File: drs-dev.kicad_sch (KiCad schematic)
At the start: 32 parts, among them J1 Conn_01x03_Pin, J2 USB_C_Receptacle_USB2.0_16P, J3 Conn_ARM_SWD_TagConnect_TC203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, J4 Conn_01x03_Pin, J5 Conn_01x03_Pin, J6 Conn_01x03_Pin, J7 Barrel_Jack_Switch, U4 SRV05-4, U5 STM32F103C8Tx, U6 AMS1117-3.3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

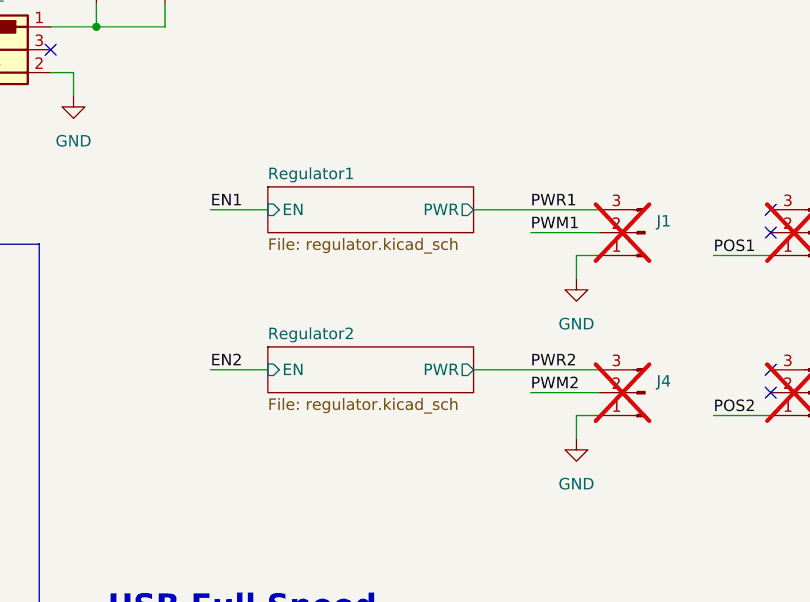
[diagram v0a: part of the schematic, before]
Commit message: Add labels and fix pinout
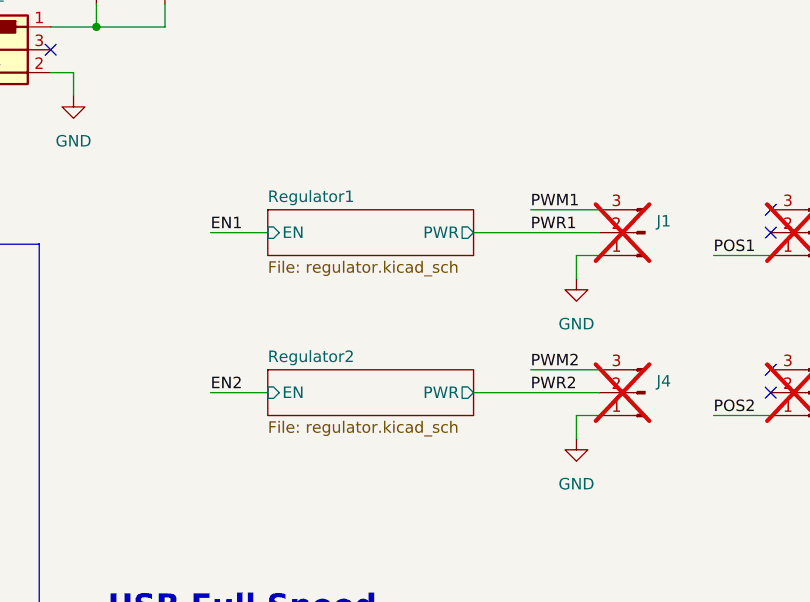
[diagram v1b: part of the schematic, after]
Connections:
- net PWM1: now also J1.3 (Pin_3); no longer J1.2 (Pin_2)
- net PWM2: now also J4.3 (Pin_3); no longer J4.2 (Pin_2)
- net PWR1: now also J1.2 (Pin_2); no longer J1.3 (Pin_3)
- net PWR2: now also J4.2 (Pin_2); no longer J4.3 (Pin_3)
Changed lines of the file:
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@@
 	(wire
 		(pts
-			(xy 187.96 69.85) (xy 195.58 69.85)
-		)
-		(stroke
-			(width 0)
-			(type default)
-		)
-	)
-	(wire
-		(pts
 			(xy 137.16 36.83) (xy 137.16 34.29)
 		)
@@
 	(wire
 		(pts
-			(xy 181.61 67.31) (xy 195.58 67.31)
+			(xy 181.61 69.85) (xy 195.58 69.85)
 		)
 		(stroke
@@
 	(wire
 		(pts
-			(xy 187.96 52.07) (xy 195.58 52.07)
+			(xy 187.96 49.53) (xy 195.58 49.53)
 		)
 		(stroke
@@
 	(wire
 		(pts
+			(xy 187.96 67.31) (xy 195.58 67.31)
+		)
+		(stroke
+			(width 0)
+			(type default)
+		)
+	)
+	(wire
+		(pts
 			(xy 40.64 166.37) (xy 48.26 166.37)
 		)
@@
 	(wire
 		(pts
-			(xy 181.61 49.53) (xy 195.58 49.53)
+			(xy 181.61 52.07) (xy 195.58 52.07)
 		)
 		(stroke
@@
 	(wire
 		(pts
-			(xy 152.4 49.53) (xy 158.75 49.53)
+			(xy 152.4 52.07) (xy 158.75 52.07)
 		)
 		(stroke
@@
 	(wire
 		(pts
-			(xy 152.4 67.31) (xy 158.75 67.31)
+			(xy 152.4 69.85) (xy 158.75 69.85)
 		)
 		(stroke
@@
 		)
 	)
-	(label "PWM2"
-		(at 187.96 69.85 0)
-		(fields_autoplaced yes)
-		(effects
-			(font
-				(size 1.27 1.27)
-			)
-			(justify left bottom)
-		)
-	)
 	(label "PWM1"
-		(at 187.96 52.07 0)
+		(at 187.96 49.53 0)
 		(fields_autoplaced yes)
 		(effects
@@
 	)
 	(label "PWR1"
-		(at 187.96 49.53 0)
+		(at 187.96 52.07 0)
 		(fields_autoplaced yes)
 		(effects
@@
 		)
 	)
+	(label "PWM2"
+		(at 187.96 67.31 0)
+		(fields_autoplaced yes)
+		(effects
+			(font
+				(size 1.27 1.27)
+			)
+			(justify left bottom)
+		)
+	)
 	(label "USB_D+"
 		(at 207.01 137.16 0)
@@
 	)
 	(label "PWR2"
-		(at 187.96 67.31 0)
+		(at 187.96 69.85 0)
 		(fields_autoplaced yes)
 		(effects
@@
 	)
 	(label "EN1"
-		(at 152.4 49.53 0)
+		(at 152.4 52.07 0)
 		(fields_autoplaced yes)
 		(effects
@@
 	)
 	(label "EN2"
-		(at 152.4 67.31 0)
+		(at 152.4 69.85 0)
 		(fields_autoplaced yes)
 		(effects
@@
 	)
 	(sheet
-		(at 158.75 46.99)
+		(at 158.75 49.53)
 		(size 22.86 5.08)
 		(fields_autoplaced yes)
@@
 		)
 		(property "Sheetname" "Regulator1"
-			(at 158.75 46.2784 0)
+			(at 158.75 48.8184 0)
 			(effects
 				(font
@@
 		)
 		(property "Sheetfile" "regulator.kicad_sch"
-			(at 158.75 52.6546 0)
+			(at 158.75 55.1946 0)
 			(effects
 				(font
@@
 		)
 		(pin "EN" input
-			(at 158.75 49.53 180)
+			(at 158.75 52.07 180)
 			(effects
 				(font
@@
 		)
 		(pin "PWR" output
-			(at 181.61 49.53 0)
+			(at 181.61 52.07 0)
 			(effects
 				(font
@@
 		)
 		(instances
-			(project "aero-dev"
+			(project "drs-dev"
 				(path "/66932111-2507-475e-a4ae-78de41b9a81d"
 					(page "2")
@@
 	)
 	(sheet
-		(at 158.75 64.77)
+		(at 158.75 67.31)
 		(size 22.86 5.08)
 		(fields_autoplaced yes)
@@
 		)
 		(property "Sheetname" "Regulator2"
-			(at 158.75 64.0584 0)
+			(at 158.75 66.5984 0)
 			(effects
 				(font
@@
 		)
 		(property "Sheetfile" "regulator.kicad_sch"
-			(at 158.75 70.4346 0)
+			(at 158.75 72.9746 0)
 			(effects
 				(font
@@
 		)
 		(pin "EN" input
-			(at 158.75 67.31 180)
+			(at 158.75 69.85 180)
 			(effects
 				(font
@@
 		)
 		(pin "PWR" output
-			(at 181.61 67.31 0)
+			(at 181.61 69.85 0)
 			(effects
 				(font
@@
 		)
 		(instances
-			(project "aero-dev"
+			(project "drs-dev"
 				(path "/66932111-2507-475e-a4ae-78de41b9a81d"
 					(page "3")

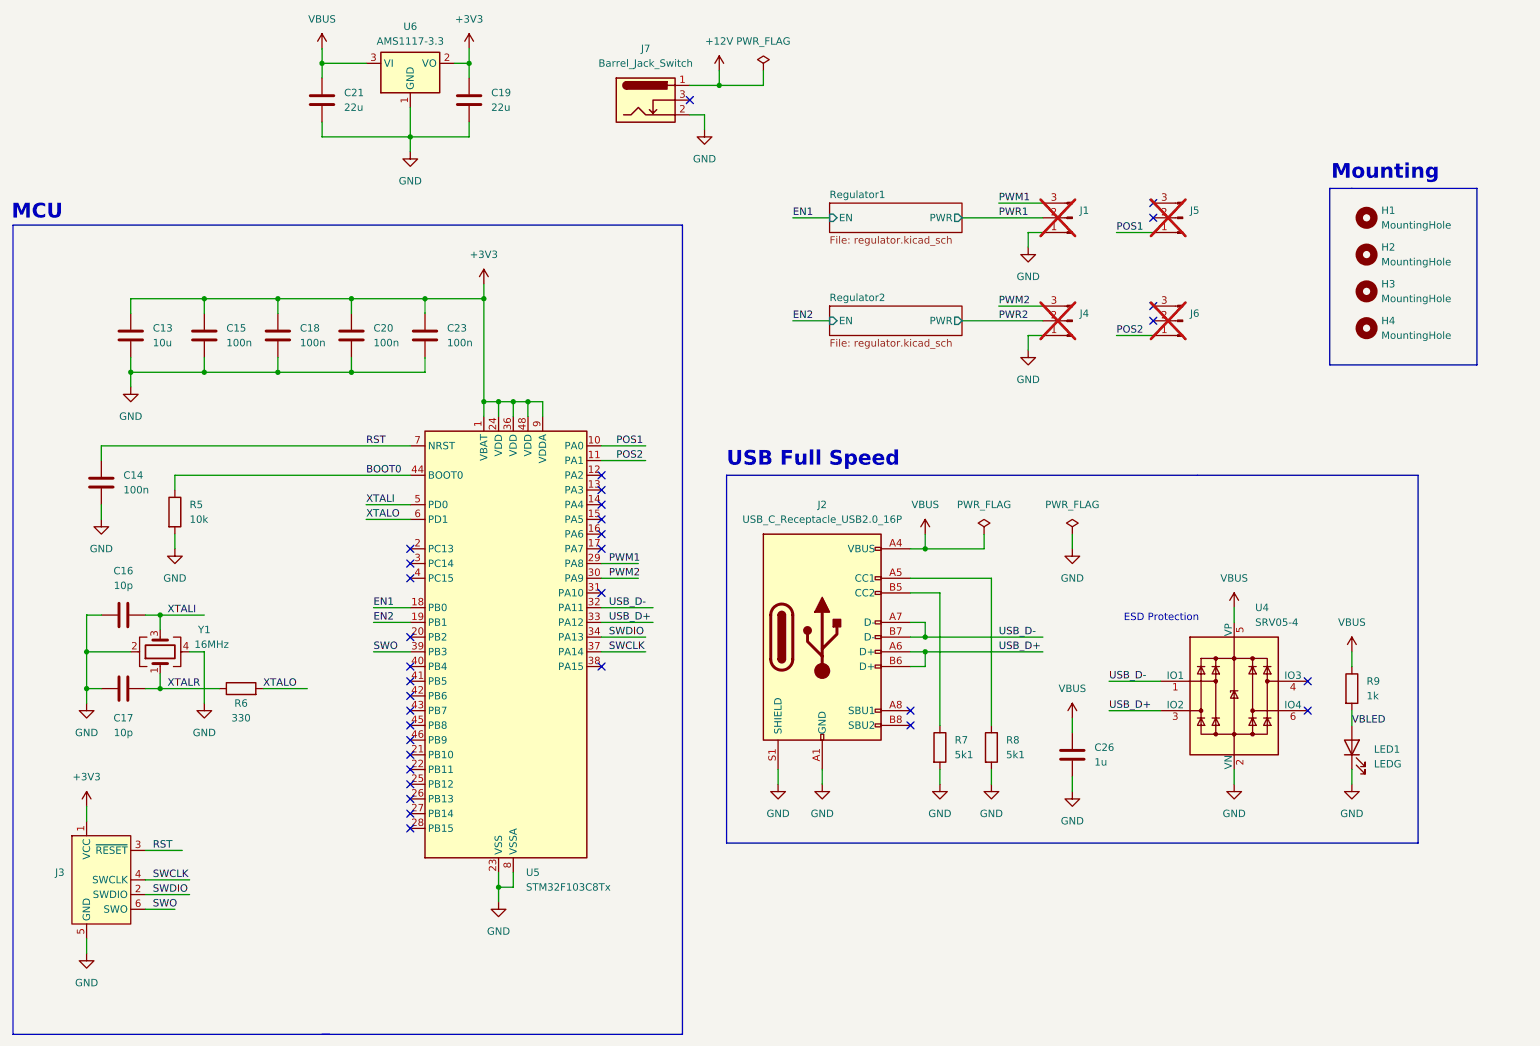
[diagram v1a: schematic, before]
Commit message: Fix usb pullup and generate new fab files
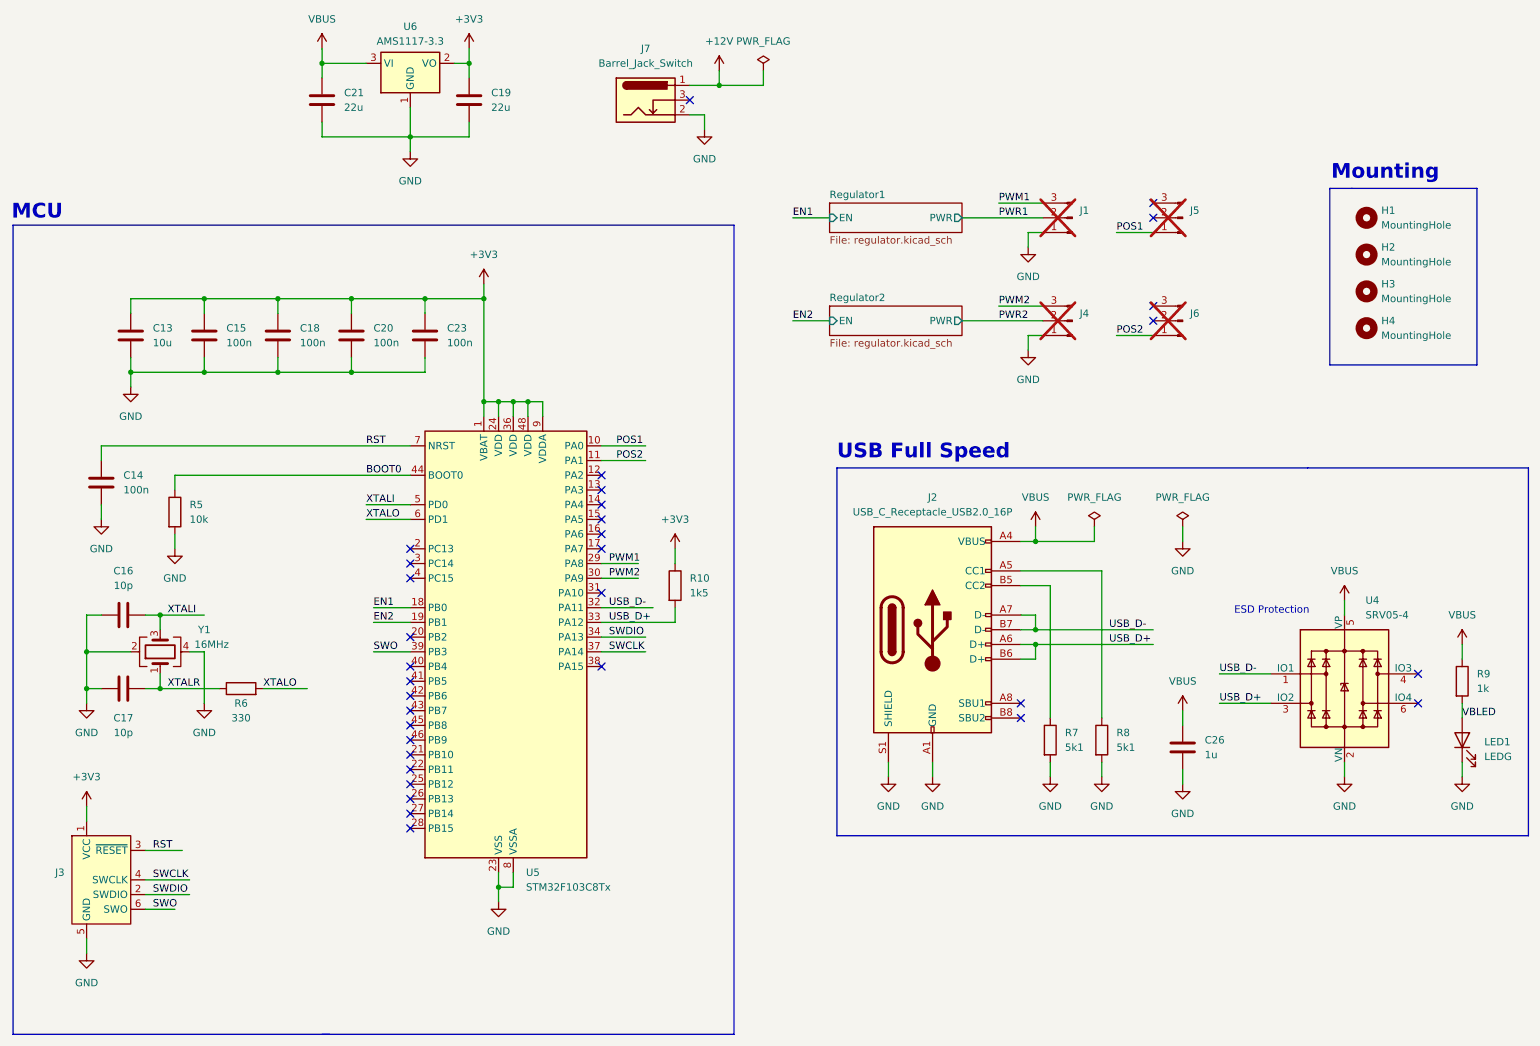
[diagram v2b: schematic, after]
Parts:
- added R10: 1k5, Resistor_SMD:R_0402_1005Metric, symbol Device:R
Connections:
- net +3V3: now also R10.1
- net USB_D+: now also R10.2
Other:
- moved on the sheet: C26, J2, LED1, R7, R8, R9, U4
